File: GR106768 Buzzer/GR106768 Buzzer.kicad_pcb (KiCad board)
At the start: 4 copper layers, 76 x 58 mm, 269 parts, among them IC1 L-BC-SOT23-5, IC2 L-BC-SO08, IC3 L-BC-SO08, IC4 L-BC-SOT23-5, IC5 L-BC-SO08, IC6 L-BC-SO08, IC7 L-BC-SOT23-6, IC8 L-BC-DFN10, IC9 L-BC-SOT23-6, J1 BAR-10-1007, J2 MIRECMS, J3 MIRECMS, SW1 SI-10-NK236, T1 Q-BC-SOT23-BEC, T10 Q-BC-SOT23-GSD, T11 Q-BC-SOT23-GSD, T12 Q-BC-SOT23-GSD, T13 Q-BC-SOT23-GSD, T2 Q-BC-SOT23-BEC, T3 Q-BC-SOT23-BEC, T4 Q-BC-SOT23-BEC, T5 Q-BC-SOT23-GSD, T6 Q-BC-SOT23-GSD, T7 Q-BC-SOT23-GSD, T8 Q-BC-SOT23-GSD, T9 Q-BC-SOT23-GSD

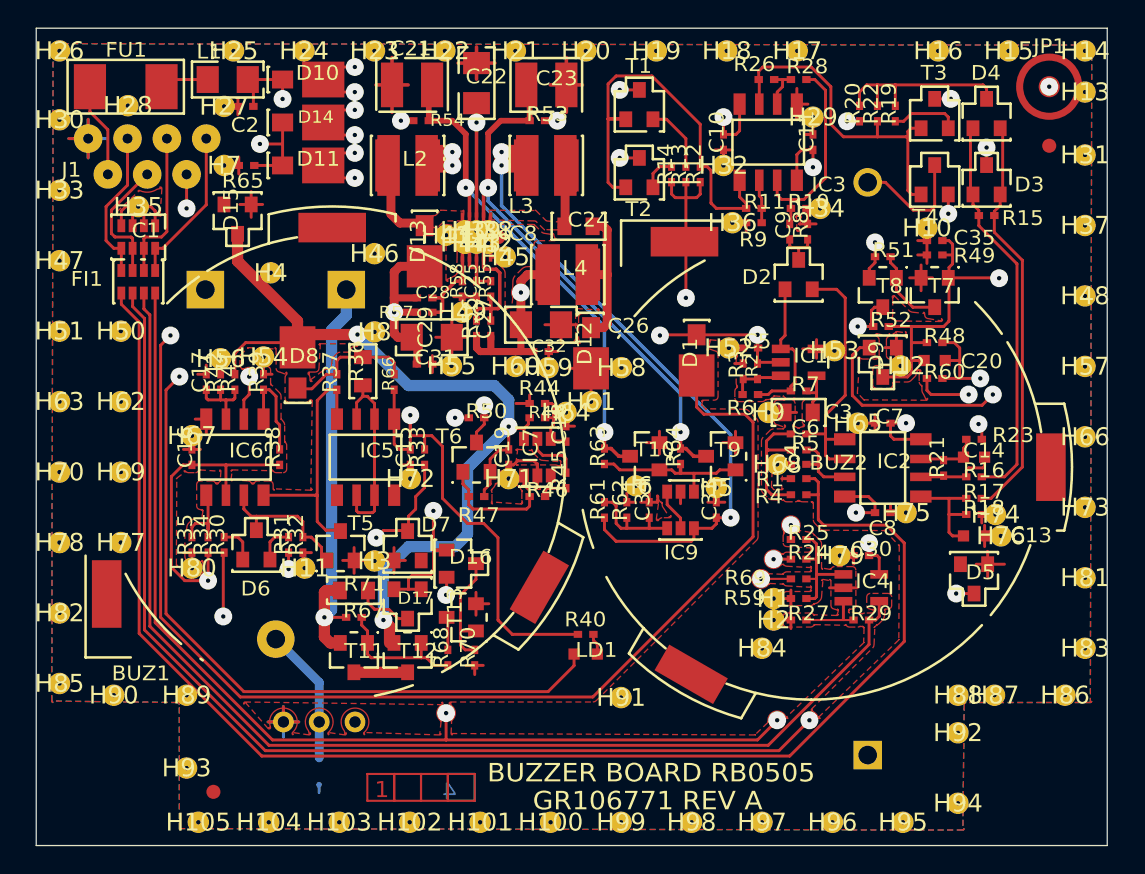
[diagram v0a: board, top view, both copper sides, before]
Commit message: hide holes
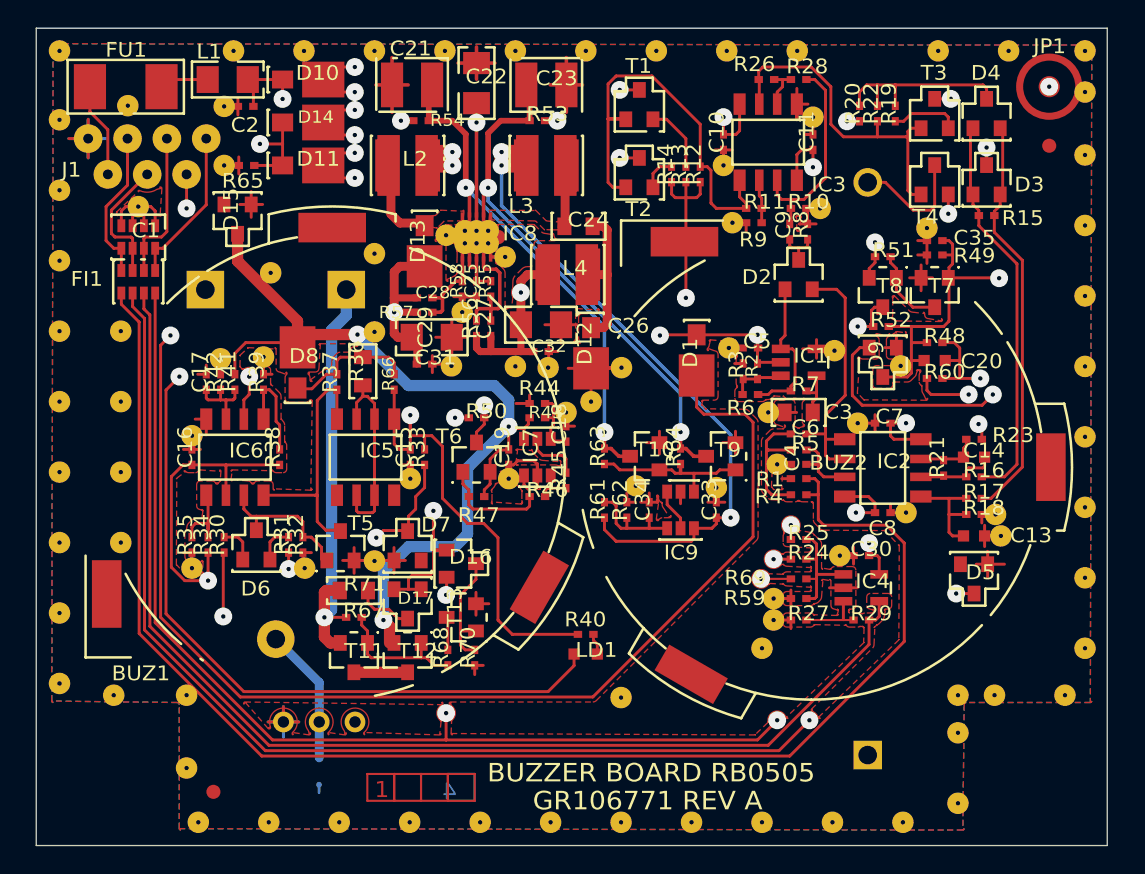
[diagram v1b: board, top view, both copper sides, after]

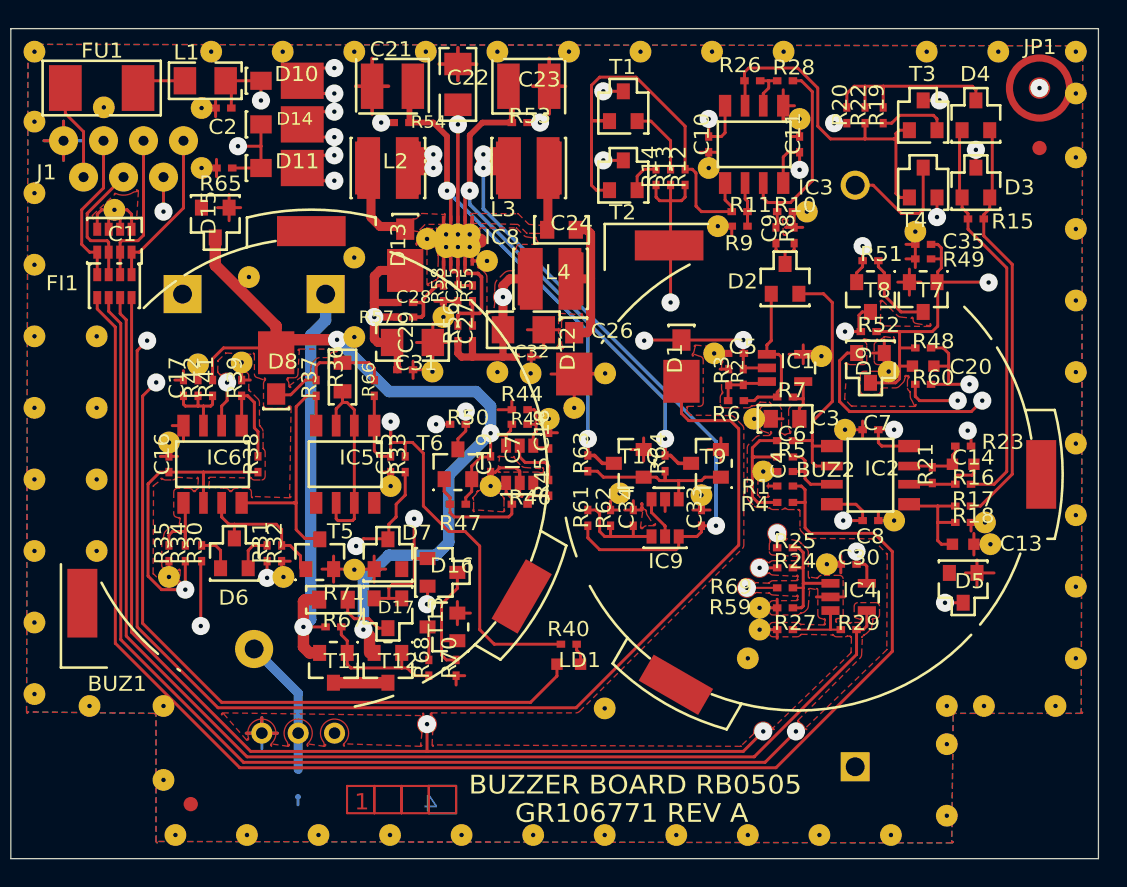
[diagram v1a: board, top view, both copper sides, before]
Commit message: update pcb based on global fp libraries
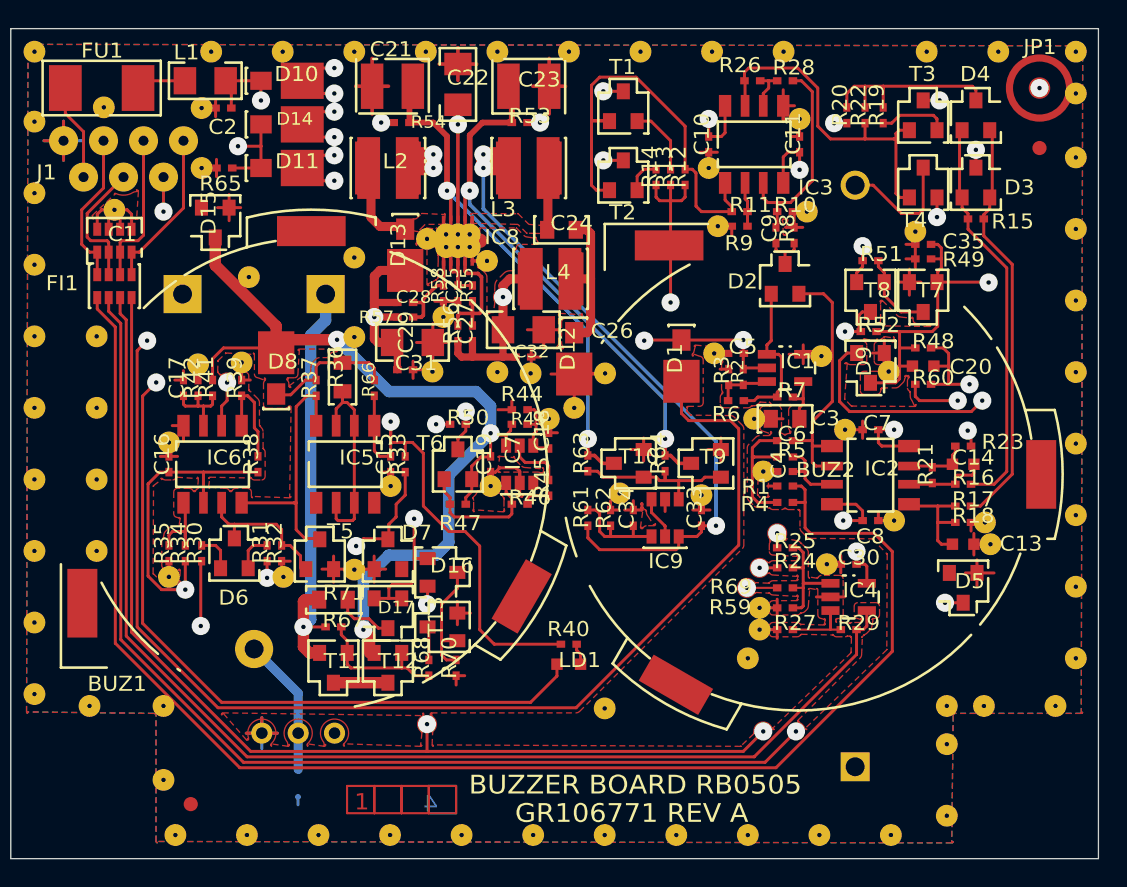
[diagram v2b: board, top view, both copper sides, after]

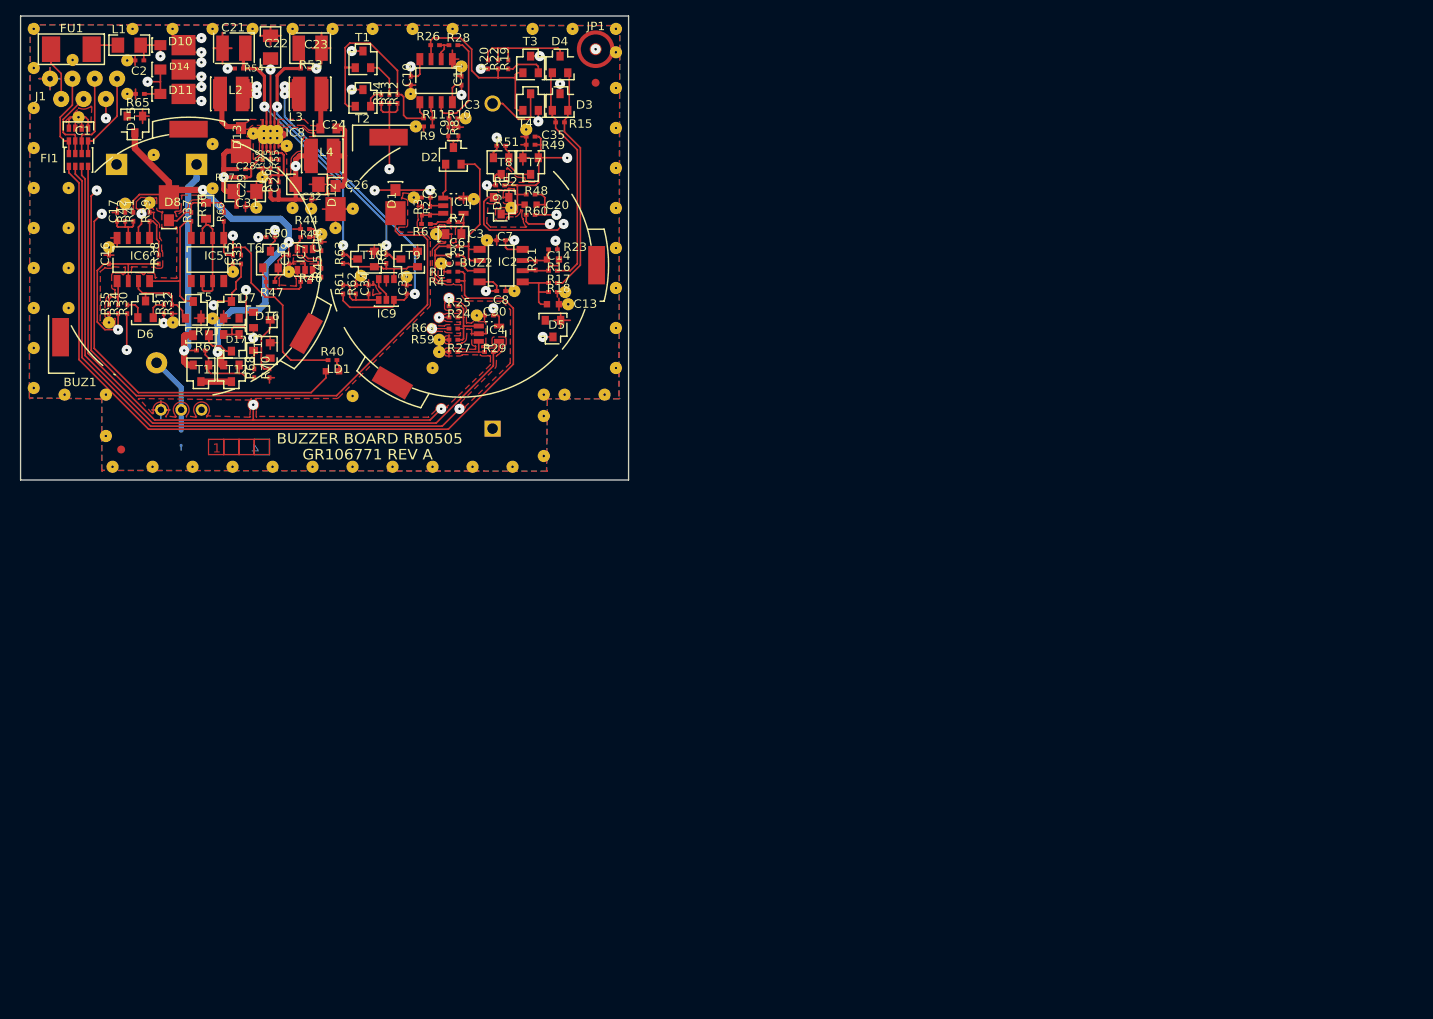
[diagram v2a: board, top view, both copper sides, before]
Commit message: changed pads to vias
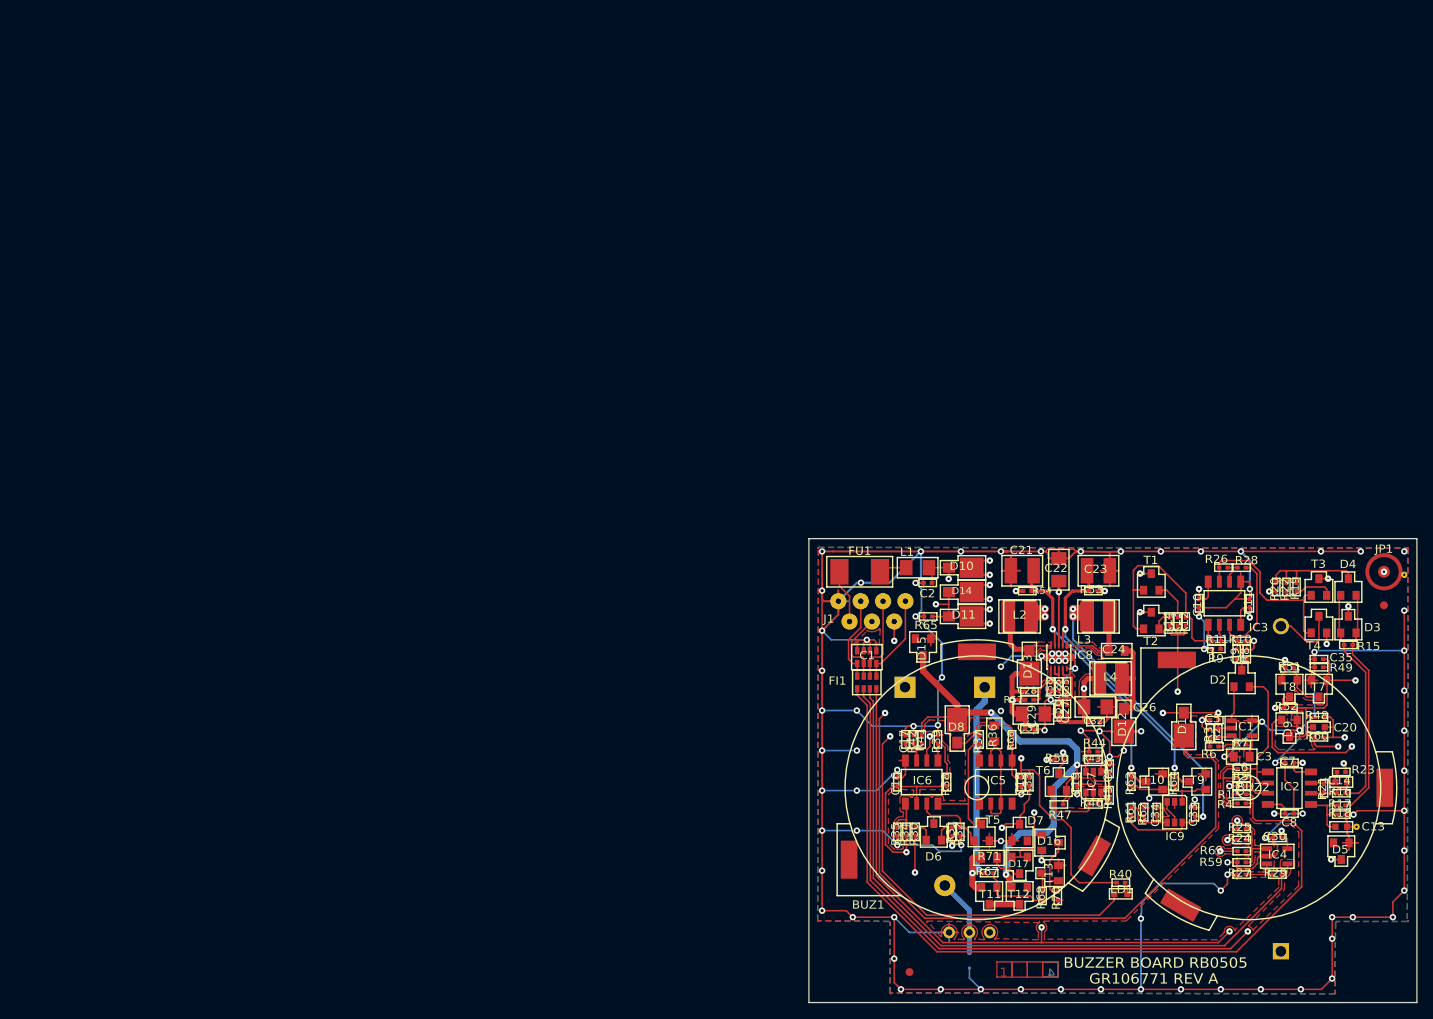
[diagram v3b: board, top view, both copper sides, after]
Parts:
- removed H1, H10, H100, H101, H102, H103, H104, H105, H11, H12, H13, H14, H15, H16, H17, H18, H19, H2, H20, H21, H22, H23, H24, H25, H26, H27, H28, H29, H3, H30, H31, H32, H33, H34, H35, H36, H37, H38, H39, H4, H40, H41, H42, H43, H44, H45, H46, H47, H48, H49, H5, H50, H51, H52, H53, H54, H55, H56, H57, H58, H59, H6, H60, H61, H62, H63, H64, H65, H66, H67, H68, H69, H7, H70, H71, H72, H73, H74, H75, H76, H77, H78, H79, H8, H80, H81, H82, H83, H84, H85, H86, H87, H88, H89, H9, H90, H91, H92, H93, H94, H95, H96, H97, H98, H99: , AllModules:ThroughHole_60milx12mil_Pad_Cu_Mask
- removed ZL2: SF-BC-NR4018, AllModules:NR4018_1
- removed ZL3, ZL4: SF-BC-NR4012, AllModules:NR4012_1
- added ?: , , F.Cu at (189.5, 69.9)
- added ?: , , F.Cu at (245.7, 54.8)
- added ?: , , F.Cu at (251.0, 33.3)
- added ?: , , F.Cu at (291.1, 33.6)
- added ?: , , F.Cu at (246.9, 34.7)
- added ?: , , F.Cu at (242.0, 34.7)
- added ?: , , F.Cu at (274.9, 35.7)
- added ?: , , F.Cu at (267.8, 36.4)
- added ?: , , F.Cu at (260.9, 36.4)
- added ?: , , F.Cu at (226.2, 36.4)
- added ?: , , F.Cu at (222.6, 36.1)
- added ?: , , F.Cu at (218.3, 36.1)
- added ?: , , F.Cu at (241.3, 56.6)
- added ?: , , F.Cu at (265.8, 37.3)
- added ?: , , F.Cu at (273.3, 37.5)
- added ?: , , F.Cu at (232.8, 37.9)
- added ?: , , F.Cu at (246.1, 38.5)
- added ?: , , F.Cu at (229.7, 38.0)
- added ?: , , F.Cu at (291.1, 38.6)
- added ?: , , F.Cu at (258.2, 38.7)
- added ?: , , F.Cu at (253.0, 38.7)
- added ?: , , F.Cu at (250.6, 38.6)
- added ?: , , F.Cu at (283.6, 39.4)
- added ?: , , F.Cu at (240.8, 50.7)
- added ?: , , F.Cu at (231.7, 39.3)
- added ?: , , F.Cu at (226.8, 39.3)
- added ?: , , F.Cu at (284.5, 40.6)
- added ?: , , F.Cu at (282.8, 40.6)
- added ?: , , F.Cu at (256.0, 41.1)
- added ?: , , F.Cu at (248.4, 41.3)
- added ?: , , F.Cu at (222.6, 41.1)
- added ?: , , F.Cu at (218.3, 41.1)
- added ?: , , F.Cu at (254.2, 41.8)
- added ?: , , F.Cu at (246.3, 42.2)
- added ?: , , F.Cu at (240.6, 52.4)
- added ?: , , F.Cu at (243.2, 42.0)
- added ?: , , F.Cu at (283.5, 42.7)
- added ?: , , F.Cu at (278.4, 42.6)
- added ?: , , F.Cu at (274.9, 42.6)
- added ?: , , F.Cu at (250.2, 42.9)
- added ?: , , F.Cu at (291.1, 43.6)
- added ?: , , F.Cu at (227.7, 43.5)
- added ?: , , F.Cu at (269.2, 45.5)
- added ?: , , F.Cu at (222.6, 46.1)
- added ?: , , F.Cu at (218.3, 46.1)
- added ?: , , F.Cu at (228.7, 22.4)
- added ?: , , F.Cu at (250.2, 46.5)
- added ?: , , F.Cu at (243.2, 46.5)
- added ?: , , F.Cu at (291.1, 48.6)
- added ?: , , F.Cu at (284.7, 49.1)
- added ?: , , F.Cu at (278.4, 49.0)
- added ?: , , F.Cu at (274.8, 49.0)
- added ?: , , F.Cu at (270.2, 49.8)
- added ?: , , F.Cu at (285.1, 50.6)
- added ?: , , F.Cu at (275.7, 51.1)
- added ?: , , F.Cu at (222.6, 51.1)
- added ?: , , F.Cu at (227.3, 25.0)
- added ?: , , F.Cu at (218.3, 51.1)
- added ?: , , F.Cu at (273.7, 52.0)
- added ?: , , F.Cu at (269.0, 52.3)
- added ?: , , F.Cu at (234.5, 53.0)
- added ?: , , F.Cu at (227.7, 52.9)
- added ?: , , F.Cu at (291.1, 53.6)
- added ?: , , F.Cu at (281.9, 54.7)
- added ?: , , F.Cu at (218.3, 56.1)
- added ?: , , F.Cu at (291.1, 58.6)
- added ?: , , F.Cu at (268.1, 58.6)
- added ?: , , F.Cu at (225.9, 22.4)
- added ?: , , F.Cu at (218.3, 61.1)
- added ?: , , F.Cu at (289.6, 61.9)
- added ?: , , F.Cu at (284.6, 61.9)
- added ?: , , F.Cu at (282.0, 61.9)
- added ?: , , F.Cu at (227.3, 61.9)
- added ?: , , F.Cu at (222.1, 61.9)
- added ?: , , F.Cu at (258.1, 62.1)
- added ?: , , F.Cu at (271.5, 63.7)
- added ?: , , F.Cu at (270.3, 63.7)
- added ?: , , F.Cu at (269.2, 63.7)
- added ?: , , F.Cu at (224.5, 25.0)
- added ?: , , F.Cu at (282.0, 64.6)
- added ?: , , F.Cu at (227.3, 67.1)
- added ?: , , F.Cu at (282.0, 69.6)
- added ?: , , F.Cu at (278.1, 70.9)
- added ?: , , F.Cu at (273.1, 70.9)
- added ?: , , F.Cu at (268.1, 70.9)
- added ?: , , F.Cu at (263.1, 70.9)
- added ?: , , F.Cu at (258.1, 70.9)
- added ?: , , F.Cu at (253.1, 70.9)
- added ?: , , F.Cu at (248.1, 70.9)
- added ?: , , F.Cu at (223.1, 22.4)
- added ?: , , F.Cu at (243.1, 70.9)
- added ?: , , F.Cu at (238.1, 70.9)
- added ?: , , F.Cu at (233.1, 70.9)
- added ?: , , F.Cu at (228.1, 70.9)
- added ?: , , F.Cu at (275.6, 25.5)
- added ?: , , F.Cu at (275.6, 66.2)
- added ?: , , F.Cu at (228.6, 33.1)
- added ?: , , F.Cu at (233.6, 57.9)
- added ?: , , F.Cu at (238.6, 33.1)
- added ?: , , F.Cu at (234.2, 63.8)
- added ?: , , F.Cu at (221.7, 25.0)
- added ?: , , F.Cu at (239.2, 63.8)
- added ?: , , F.Cu at (236.7, 63.8)
- added ?: , , F.Cu at (116.0, 150.4)
- added ?: , , F.Cu at (116.0, 145.3)
- added ?: , , F.Cu at (116.0, 155.1)
- added ?: , , F.Cu at (116.0, 140.3)
- added ?: , , F.Cu at (183.5, 101.4)
- added ?: , , F.Cu at (220.3, 22.4)
- added ?: , , F.Cu at (233.3, 31.9)
- added ?: , , F.Cu at (256.9, 43.2)
- added ?: , , F.Cu at (262.3, 43.2)
- added ?: , , F.Cu at (265.9, 49.3)
- added ?: , , F.Cu at (264.9, 47.2)
- added ?: , , F.Cu at (259.2, 47.1)
- added ?: , , F.Cu at (248.7, 25.9)
- added ?: , , F.Cu at (247.1, 25.9)
- added ?: , , F.Cu at (249.6, 24.3)
- added ?: , , F.Cu at (239.4, 36.3)
- added ?: , , F.Cu at (246.1, 24.3)
- added ?: , , F.Cu at (246.1, 23.4)
- added ?: , , F.Cu at (242.5, 21.1)
- added ?: , , F.Cu at (247.9, 21.3)
- added ?: , , F.Cu at (253.6, 21.1)
- added ?: , , F.Cu at (230.0, 24.3)
- added ?: , , F.Cu at (240.6, 36.1)
- added ?: , , F.Cu at (229.9, 56.3)
- added ?: , , F.Cu at (249.6, 23.4)
- added ?: , , F.Cu at (268.6, 41.8)
- added ?: , , F.Cu at (237.1, 56.4)
- added ?: , , F.Cu at (279.8, 28.8)
- added ?: , , F.Cu at (285.0, 32.3)
- added ?: , , F.Cu at (262.7, 33.7)
- added ?: , , F.Cu at (235.7, 52.9)
- added ?: , , F.Cu at (228.8, 53.8)
- added ?: , , F.Cu at (278.0, 38.5)
- added ?: , , F.Cu at (291.1, 19.1)
- added ?: , , F.Cu at (291.1, 16.2)
- added ?: , , F.Cu at (285.6, 16.2)
- added ?: , , F.Cu at (280.6, 16.2)
- added ?: , , F.Cu at (268.1, 53.7)
- added ?: , , F.Cu at (270.6, 16.2)
- added ?: , , F.Cu at (265.6, 16.2)
- added ?: , , F.Cu at (260.6, 16.2)
- added ?: , , F.Cu at (255.6, 16.2)
- added ?: , , F.Cu at (250.6, 16.2)
- added ?: , , F.Cu at (245.6, 16.2)
- added ?: , , F.Cu at (240.6, 16.2)
- added ?: , , F.Cu at (235.6, 16.2)
- added ?: , , F.Cu at (230.6, 16.2)
- added ?: , , F.Cu at (218.3, 16.2)
- added ?: , , F.Cu at (269.0, 55.1)
- added ?: , , F.Cu at (239.2, 17.3)
- added ?: , , F.Cu at (288.5, 18.7)
- added ?: , , F.Cu at (258.0, 19.0)
- added ?: , , F.Cu at (239.2, 19.1)
- added ?: , , F.Cu at (281.5, 19.6)
- added ?: , , F.Cu at (234.1, 19.6)
- added ?: , , F.Cu at (230.0, 20.1)
- added ?: , , F.Cu at (223.1, 20.1)
- added ?: , , F.Cu at (239.2, 20.4)
- added ?: , , F.Cu at (274.2, 21.2)
- added ?: , , F.Cu at (269.0, 56.6)
- added ?: , , F.Cu at (271.7, 20.9)
- added ?: , , F.Cu at (265.4, 20.9)
- added ?: , , F.Cu at (218.3, 21.1)
- added ?: , , F.Cu at (239.2, 22.2)
- added ?: , , F.Cu at (284.1, 23.0)
- added ?: , , F.Cu at (232.5, 22.8)
- added ?: , , F.Cu at (291.1, 23.6)
- added ?: , , F.Cu at (258.0, 23.8)
- added ?: , , F.Cu at (239.2, 23.4)
- added ?: , , F.Cu at (271.7, 24.4)
- added ?: , , F.Cu at (245.7, 63.2)
- added ?: , , F.Cu at (265.4, 24.3)
- added ?: , , F.Cu at (239.2, 25.2)
- added ?: , , F.Cu at (218.3, 26.1)
- added ?: , , F.Cu at (281.3, 27.7)
- added ?: , , F.Cu at (272.3, 27.4)
- added ?: , , F.Cu at (227.3, 27.4)
- added ?: , , F.Cu at (223.9, 27.2)
- added ?: , , F.Cu at (266.0, 28.4)
- added ?: , , F.Cu at (291.1, 28.6)
- added ?: , , F.Cu at (248.7, 29.0)
- added ?: , , F.Cu at (244.8, 48.8)
- added ?: , , F.Cu at (247.9, 29.0)
- added ?: , , F.Cu at (247.0, 29.0)
- added ?: , , F.Cu at (245.7, 29.3)
- added ?: , , F.Cu at (276.1, 29.8)
- added ?: , , F.Cu at (248.7, 29.9)
- added ?: , , F.Cu at (247.9, 29.9)
- added ?: , , F.Cu at (247.0, 29.9)
- added ?: , , F.Cu at (249.9, 30.8)
- added ?: , , F.Cu at (240.6, 30.6)
- added ?: , , F.Cu at (218.3, 31.1)
- added CAM1: A3_EQFC_COVIDIEN, A3_EQFC_COVIDIEN_1, F.Cu at (245.1, 58.2)
- added CAM12: FABRICATION, FABRICATION_1, F.Cu at (109.8, 0.01)
- added CAM13: PERCAGE_TABLEAU, PERCAGE_TABLEAU_1, F.Cu at (109.9, 121.1)
- added CAM14: A3_PER_COVIDIEN, A3_PER_COVIDIEN_1, F.Cu at (206.1, 83.5)
- added CAM2: PER-COVIDIEN_TEXTE, PER-COVIDIEN_TEXTE_1, F.Cu at (222.5, 92.1)
- added CAM3: A3_EQFS_COVIDIEN, A3_EQFS_COVIDIEN_1, B.Cu at (278.0, 57.7)
- added CAM5: FILM13_HORIZONTAL, FILM13_HORIZONTAL_1, F.Cu at (251.2, 46.3)
- added CAM6: COIN_EXTERNE, COIN_EXTERNE_1, F.Cu at (216.6, 14.6)
- added CAM7: COIN_EXTERNE, COIN_EXTERNE_1, F.Cu at (216.6, 72.6)
- added CAM8: COIN_EXTERNE, COIN_EXTERNE_1, F.Cu at (292.6, 72.6)
- added CAM9: COIN_EXTERNE, COIN_EXTERNE_1, F.Cu at (292.6, 14.6)
- added L2-2: SF-BC-NR4018, NR4018_1, F.Cu at (141.4, 75.1)
- added L3-2: SF-BC-NR4012, NR4012_1, F.Cu at (151.2, 75.1)
- added L4-2: SF-BC-NR4012, NR4012_1, F.Cu at (152.7, 82.9)
- BAT1: footprint AllModules:BT-4-V150H-4.8V_1 -> BT-4-V150H-4.8V_1
- BUZ1, BUZ2: footprint AllModules:PKM33EPH-1201C_1 -> PKM33EPH-1201C_1
- C1: footprint AllModules:C0612-4_1 -> C0612-4_1
- C10, C11, C15, C16, C17, C18, C19, C2, C25, C27, C28, C30, C31, C32, C33, C34, C35, C4, C5, C6, C7, C8, C9: footprint AllModules:C0402_1b -> C0402_1
- C12: footprint AllModules:AX10X30_1 -> AX10X30_1
- C13, C14, C20: footprint AllModules:C0603_1b -> C0603_1
- C21, C23: footprint AllModules:C1210_1 -> C1210_1
- C22, C26, C29, L1: footprint AllModules:RC1206_1 -> RC1206_1
- C24, C3: footprint AllModules:C0805_1b -> C0805_1
- D1, D10, D11, D12, D13, D14, D8: footprint AllModules:DO216AA_1 -> DO216AA_1
- D15, D16, D17, D2, D3, D4, D5, D6, D7, D9: footprint AllModules:SOT23-1G_1 -> SOT23-1G_1
- FI1: footprint AllModules:WE-FA_1 -> WE-FA_1
- FU1: footprint AllModules:F6126_1 -> F6126_1
- IC1, IC4: footprint AllModules:SOT23-5_1 -> SOT23-5_1
- IC2, IC3, IC5, IC6: footprint AllModules:MX.A8_COMPOSANT_1 -> MX.A8_COMPOSANT_1
- IC7, IC9: footprint AllModules:SOT23-6_1 -> SOT23-6_1
- IC8: footprint AllModules:DFN10_1 -> DFN10_1
- J1: footprint AllModules:BAR7-3-2-COVIDIEN_1 -> BAR7-3-2-COVIDIEN_1
- J2, J3: footprint AllModules:MIRECMS-SAFT_1 -> MIRECMS-SAFT_1
- JP1: footprint AllModules:TB-CMS-AIROX_1 -> TB-CMS-AIROX_1
- L2, L3, L4: footprint AllModules:WETPC-S_1 -> WETPC-S_1
- LD1: footprint AllModules:D0603_1 -> D0603_1
- R1, R10, R11, R12, R13, R14, R15, R16, R17, R18, R19, R2, R20, R21, R22, R23, R24, R25, R26, R27, R28, R29, R3, R30, R31, R32, R33, R34, R35, R37, R38, R39, R4, R40, R41, R42, R43, R44, R45, R46, R47, R48, R49, R5, R50, R51, R52, R53, R54, R55, R56, R57, R58, R59, R6, R60, R61, R62, R63, R64, R65, R66, R67, R68, R69, R7, R70, R8, R9: footprint AllModules:R0402_1 -> R0402_1
- R36, R71: footprint AllModules:R0805_1b -> R0805_1
- SJ1: footprint AllModules:TB-CMS-AIROX-2_1 -> TB-CMS-AIROX-2_1
- SW1: footprint AllModules:NK236_1_1 -> NK236_1_1
- T1, T2, T3, T4: footprint AllModules:SOT23-BEC_1 -> SOT23-BEC_1
- T10, T11, T12, T13, T5, T6, T7, T8, T9: footprint AllModules:SOT23-GSD_1 -> SOT23-GSD_1
- moved C12 118.2 mm to (174.0, 117.0)
- moved BAT1 118.2 mm to (132.0, 96.4)
- moved C33 118.2 mm to (163.3, 99.6)
- moved T10 118.2 mm to (158.2, 95.8)
- moved IC9 118.2 mm to (160.7, 99.6)
- moved R62 118.2 mm to (156.9, 99.6)
- moved R64 118.2 mm to (160.7, 95.8)
- moved T5 118.2 mm to (136.6, 102.1)
- moved BUZ1 118.2 mm to (136.0, 96.5)
- moved SJ1 118.2 mm to (135.1, 118.3)
- moved C11 118.2 mm to (170.1, 73.5)
- moved C17 118.2 mm to (127.1, 90.5)
- moved C18 118.2 mm to (152.6, 94.2)
- moved C19 118.2 mm to (148.6, 95.8)
- moved C2 118.2 mm to (129.9, 70.9)
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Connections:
- BAT1 pad +: (no net) -> BATTV
- BAT1 pad -: (no net) -> N$20
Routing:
- net GND: track 446.8 -> 787.5 mm, vias 0 -> 103
- net N$10: track 76.6 -> 110.3 mm
- net N$46: track 4.27 -> 9.74 mm
- net N$42: track 6.11 -> 9.11 mm
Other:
- board text removed: "B"

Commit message: trying to add vias
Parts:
- removed ? (x195): , 
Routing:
- net GND: vias 103 -> 105
